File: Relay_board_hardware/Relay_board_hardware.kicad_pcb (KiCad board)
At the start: 2 copper layers, 101.6 x 101.6 mm, 25 parts, among them IC1 BTS3800SL, Q1 Q_NMOS_GDS, U1 Opamp_Dual

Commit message: moved trace and generated gerbs
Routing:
- net /RLY_V-: track 26.4 -> 27.3 mm
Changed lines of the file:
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@@
       (outputformat 1)
       (mirror false)
-      (drillshape 1)
+      (drillshape 0)
       (scaleselection 1)
-      (outputdirectory "")
+      (outputdirectory "gerbs/")
     )
   )
@@
     (fp_line (start 3.15 1.6) (end -3.15 1.6)
       (stroke (width 0.1) (type solid)) (layer "F.Fab"))
-    (pad "1" smd roundrect (at -3.05 0 180) (size 1.4 3.35) (layers "F.Cu" "F.Paste" "F.Mask") (roundrect_rratio 0.178571)
+    (pad "1" smd roundrect (at -3.05 0 180) (size 1.4 3.35) (layers "F.Cu" "F.Paste" "F.Mask") (roundrect_rratio 0.1785707143)
       (net 9 "Net-(U1A-+)") (pintype "passive"))
-    (pad "2" smd roundrect (at 3.05 0 180) (size 1.4 3.35) (layers "F.Cu" "F.Paste" "F.Mask") (roundrect_rratio 0.178571)
+    (pad "2" smd roundrect (at 3.05 0 180) (size 1.4 3.35) (layers "F.Cu" "F.Paste" "F.Mask") (roundrect_rratio 0.1785707143)
       (net 1 "GNDPWR") (pintype "passive"))
     (model "${KICAD6_3DMODEL_DIR}/Resistor_SMD.3dshapes/R_2512_6332Metric.wrl"
@@
     (fp_line (start 3.15 1.6) (end -3.15 1.6)
       (stroke (width 0.1) (type solid)) (layer "F.Fab"))
-    (pad "1" smd roundrect (at -3.05 0 180) (size 1.4 3.35) (layers "F.Cu" "F.Paste" "F.Mask") (roundrect_rratio 0.178571)
+    (pad "1" smd roundrect (at -3.05 0 180) (size 1.4 3.35) (layers "F.Cu" "F.Paste" "F.Mask") (roundrect_rratio 0.1785707143)
       (net 6 "VBUS") (pintype "passive"))
-    (pad "2" smd roundrect (at 3.05 0 180) (size 1.4 3.35) (layers "F.Cu" "F.Paste" "F.Mask") (roundrect_rratio 0.178571)
+    (pad "2" smd roundrect (at 3.05 0 180) (size 1.4 3.35) (layers "F.Cu" "F.Paste" "F.Mask") (roundrect_rratio 0.1785707143)
       (net 9 "Net-(U1A-+)") (pintype "passive"))
     (model "${KICAD6_3DMODEL_DIR}/Resistor_SMD.3dshapes/R_2512_6332Metric.wrl"
@@
     (fp_line (start 5.625 5) (end 5.625 -5)
       (stroke (width 0.1) (type solid)) (layer "B.Fab"))
-    (pad "1" smd roundrect (at -7.65 2.54 90) (size 4.6 1.1) (layers "B.Cu" "B.Paste" "B.Mask") (roundrect_rratio 0.227273)
+    (pad "1" smd roundrect (at -7.65 2.54 90) (size 4.6 1.1) (layers "B.Cu" "B.Paste" "B.Mask") (roundrect_rratio 0.2272727273)
       (net 13 "DSCHG_IN") (pinfunction "G") (pintype "input"))
-    (pad "2" smd roundrect (at -0.925 -2.775 90) (size 4.55 5.25) (layers "B.Cu" "B.Paste") (roundrect_rratio 0.054945)
+    (pad "2" smd roundrect (at -0.925 -2.775 90) (size 4.55 5.25) (layers "B.Cu" "B.Paste") (roundrect_rratio 0.05494505495)
       (net 10 "/PWRRES") (pinfunction "D") (pintype "passive"))
-    (pad "2" smd roundrect (at -0.925 2.775 90) (size 4.55 5.25) (layers "B.Cu" "B.Paste") (roundrect_rratio 0.054945)
+    (pad "2" smd roundrect (at -0.925 2.775 90) (size 4.55 5.25) (layers "B.Cu" "B.Paste") (roundrect_rratio 0.05494505495)
       (net 10 "/PWRRES") (pinfunction "D") (pintype "passive"))
-    (pad "2" smd roundrect (at 1.5 0 90) (size 9.4 10.8) (layers "B.Cu" "B.Mask") (roundrect_rratio 0.026596)
+    (pad "2" smd roundrect (at 1.5 0 90) (size 9.4 10.8) (layers "B.Cu" "B.Mask") (roundrect_rratio 0.02659595745)
       (net 10 "/PWRRES") (pinfunction "D") (pintype "passive"))
-    (pad "2" smd roundrect (at 3.925 -2.775 90) (size 4.55 5.25) (layers "B.Cu" "B.Paste") (roundrect_rratio 0.054945)
+    (pad "2" smd roundrect (at 3.925 -2.775 90) (size 4.55 5.25) (layers "B.Cu" "B.Paste") (roundrect_rratio 0.05494505495)
       (net 10 "/PWRRES") (pinfunction "D") (pintype "passive"))
-    (pad "2" smd roundrect (at 3.925 2.775 90) (size 4.55 5.25) (layers "B.Cu" "B.Paste") (roundrect_rratio 0.054945)
+    (pad "2" smd roundrect (at 3.925 2.775 90) (size 4.55 5.25) (layers "B.Cu" "B.Paste") (roundrect_rratio 0.05494505495)
       (net 10 "/PWRRES") (pinfunction "D") (pintype "passive"))
-    (pad "3" smd roundrect (at -7.65 -2.54 90) (size 4.6 1.1) (layers "B.Cu" "B.Paste" "B.Mask") (roundrect_rratio 0.227273)
+    (pad "3" smd roundrect (at -7.65 -2.54 90) (size 4.6 1.1) (layers "B.Cu" "B.Paste" "B.Mask") (roundrect_rratio 0.2272727273)
       (net 1 "GNDPWR") (pinfunction "S") (pintype "passive"))
     (model "${KICAD6_3DMODEL_DIR}/Package_TO_SOT_SMD.3dshapes/TO-263-2.wrl"
@@
   (segment (start 156.337 123.657) (end 156.754 123.24) (width 2.54) (layer "F.Cu") (net 7))
   (segment (start 156.337 133.9228) (end 156.337 123.657) (width 2.54) (layer "F.Cu") (net 7))
-  (segment (start 151.816 130.5698) (end 151.816 114.21) (width 2.54) (layer "F.Cu") (net 8))
-  (segment (start 151.816 114.21) (end 148.046 110.44) (width 2.54) (layer "F.Cu") (net 8))
-  (segment (start 148.463 133.9228) (end 151.816 130.5698) (width 2.54) (layer "F.Cu") (net 8))
+  (segment (start 152.908 129.4778) (end 152.908 115.302) (width 2.54) (layer "F.Cu") (net 8))
+  (segment (start 148.463 133.9228) (end 152.908 129.4778) (width 2.54) (layer "F.Cu") (net 8))
+  (segment (start 152.908 115.302) (end 148.046 110.44) (width 2.54) (layer "F.Cu") (net 8))
   (segment (start 163.195 95.25) (end 168.4 95.25) (width 0.254) (layer "F.Cu") (net 9))
   (segment (start 152.4 95.25) (end 147.195 95.25) (width 0.254) (layer "F.Cu") (net 9))

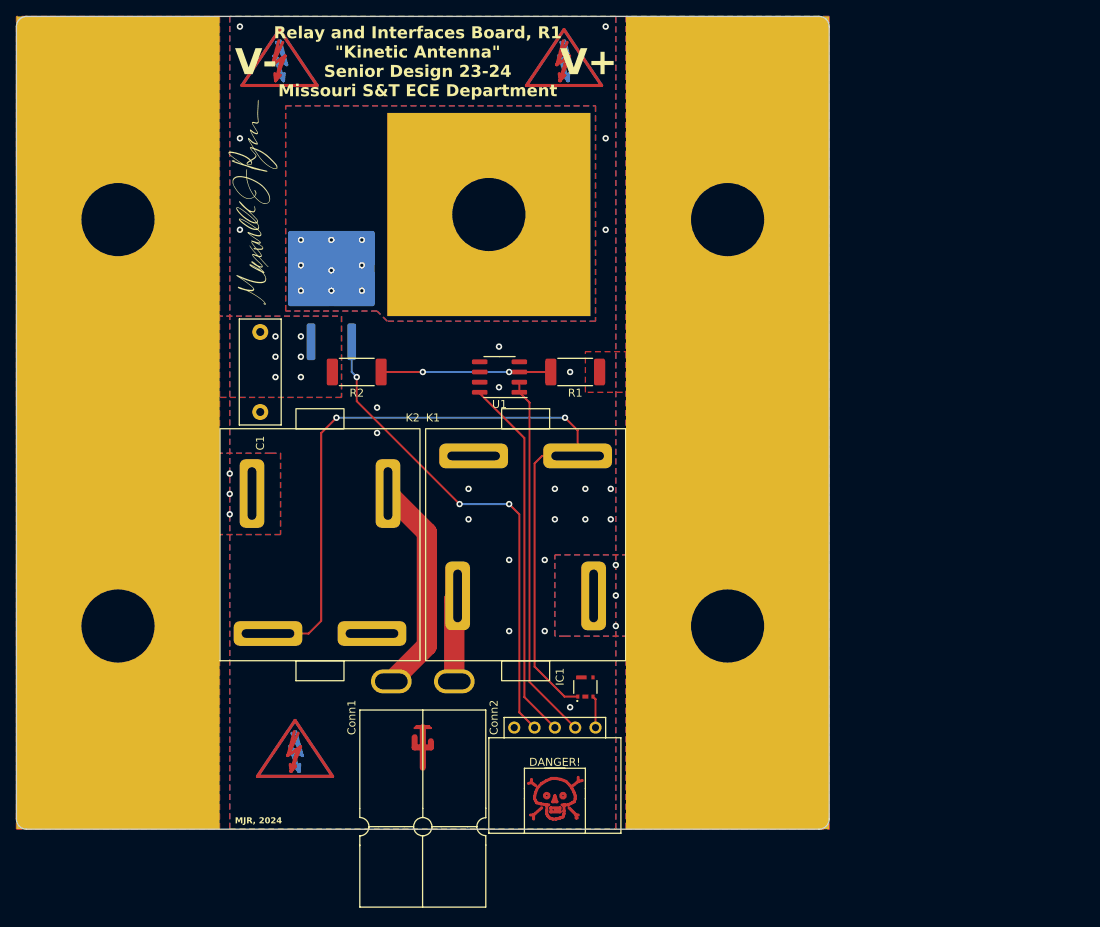
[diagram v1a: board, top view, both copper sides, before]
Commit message: 12V connection redesign
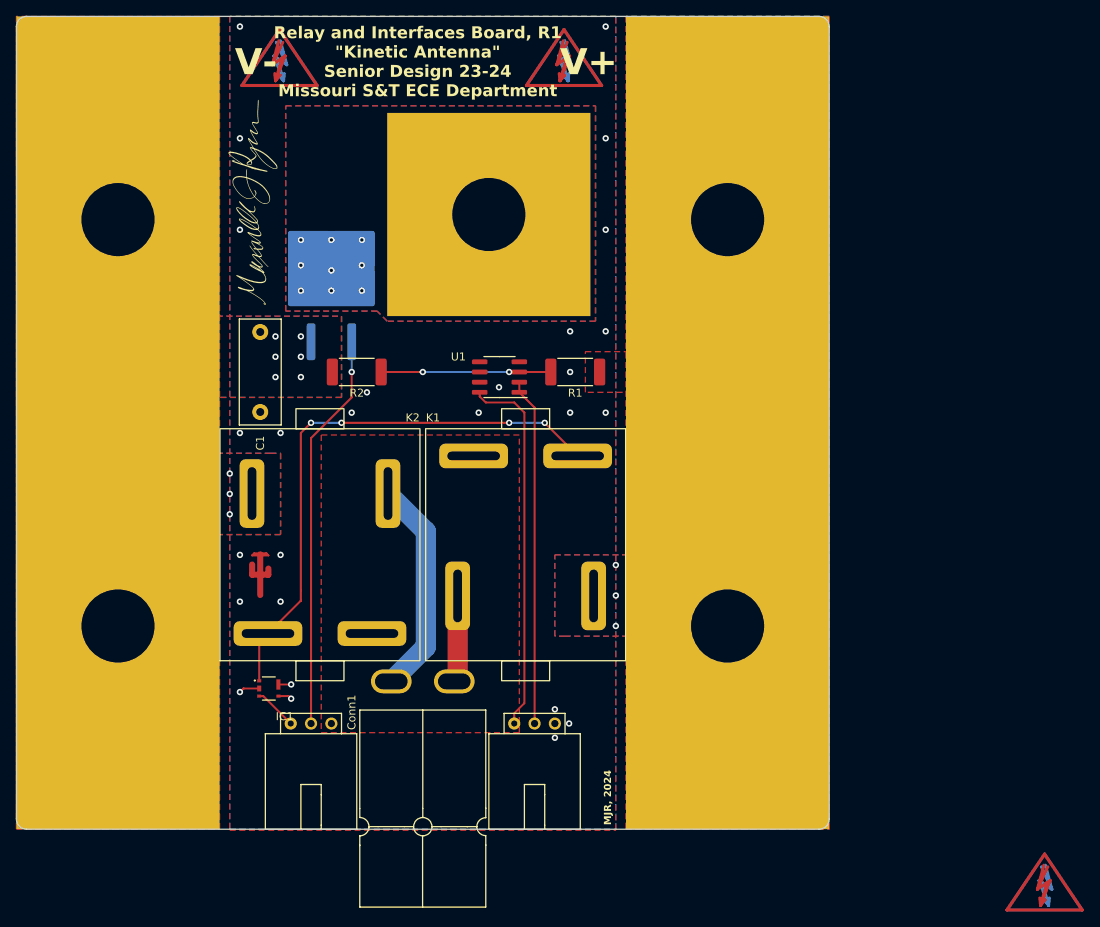
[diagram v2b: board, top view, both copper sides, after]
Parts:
- removed DANGER!: Symbol_Danger_CopperTop_Small, Symbol:Symbol_Danger_CopperTop_Small
- added Conn3: Molex_SL_03, 0-customs:MOLEX_SL_03_Horizontal, F.Cu at (141.0, 139.2)
- Conn2: value Molex_SL_05 -> Molex_SL_03; footprint 0-customs:MOLEX_SL_05_Horizontal -> 0-customs:MOLEX_SL_03_Horizontal
- Q1: value Q_NMOS_GDS -> IRF740ASPBF
- R1: value R -> 650k
- R2: value R -> 5k6
- U1: value Opamp_Dual -> MCP6497T-E/SN
- moved REF** 95.2 mm to (230.1, 159.7) (x2)
- moved IC1 39.6 mm to (133.2, 134.8), turned to -90 degrees
- moved REF** 29.6 mm to (132.1, 113.0)
- moved Conn2 5.11 mm to (168.9, 139.2)
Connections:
- Conn2 pad 1: RLY_IN -> GND
- IC1 pad 2: unconnected-(IC1-N.C._1-Pad2) -> GND
- IC1 pad 5: unconnected-(IC1-N.C._2-Pad5) -> GND
- K1 pad 1: GND -> +12V
- K2 pad 1: GND -> +12V
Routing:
- net Net-(IC1-DRAIN): track 105.6 -> 71.3 mm, vias 2 -> 4
- net DSCHG_IN: track 61.3 -> 49.8 mm, vias 3 -> 1
- net GND: track 0.00 -> 5.92 mm, vias 24 -> 27
- net /V_SENSE_OUT: track 46.1 -> 43.5 mm
- net RLY_IN: track 4.01 -> 5.36 mm
- net +3V3: track 45.8 -> 46.3 mm
- added copper zone on F.Cu, net +12V

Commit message: silkscreen updated, relay to rail plane dimensions confirmed, filecleanup,
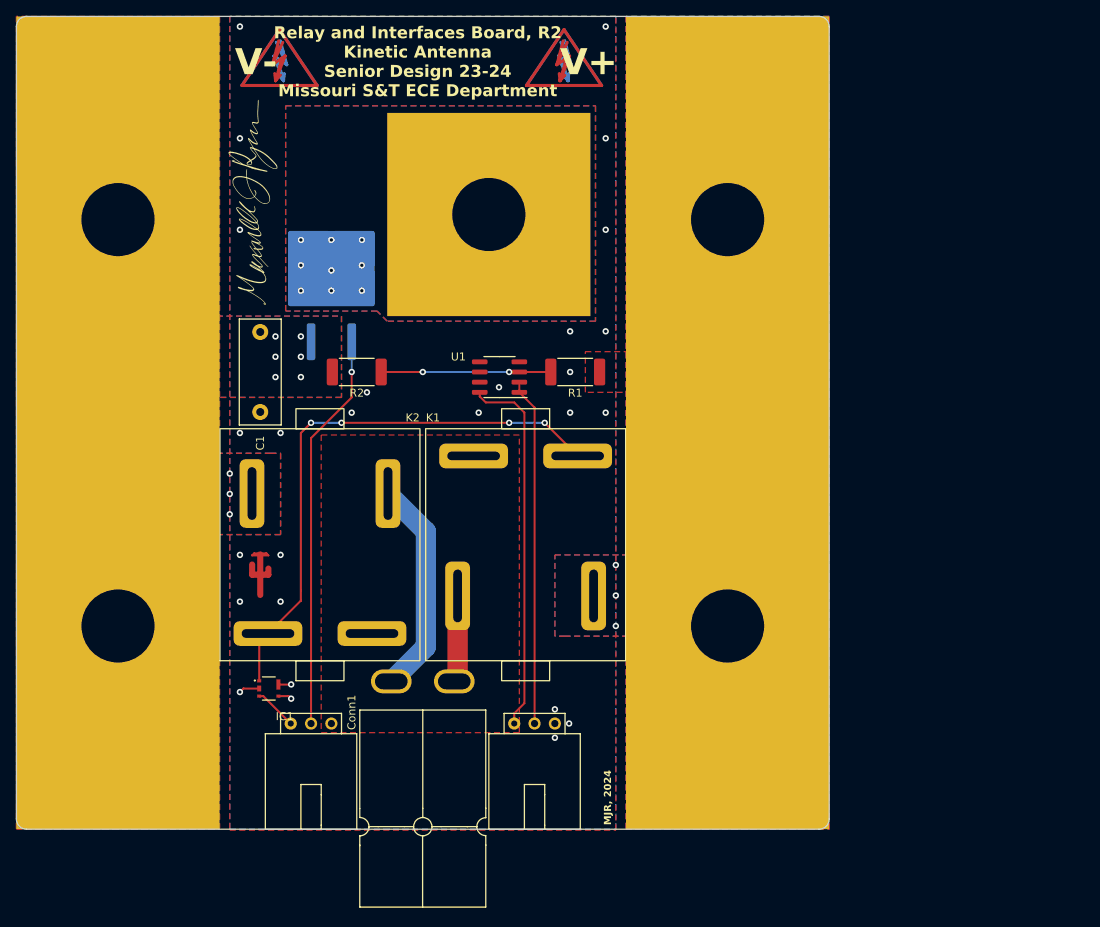
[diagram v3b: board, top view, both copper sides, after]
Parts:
- removed the G*** at (152.4, 55.9)
- removed the REF** at (230.1, 159.7) (x2)
- added G***: LOGO, MRDT_Silkscreens:yagi2_20mm, B.Cu at (152.4, 55.9)
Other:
- board text added: "Relay and Interfaces Board, R2 Kinetic Antenna Senior Design 23-24 Missouri S&T ECE Department"
- board text removed: "Relay and Interfaces Board, R1 {dblquote}Kinetic Antenna{dblquote} Senior Design 23-24 Missouri S&T ECE Department"

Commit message: R2 edits
gerbs generated
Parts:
- removed the REF** at (132.1, 113.0)
- added R3: 10k, Resistor_SMD:R_0603_1608Metric_Pad0.98x0.95mm_HandSolder, B.Cu at (145.2, 98.8)
- added U2: MCP1416, Package_TO_SOT_SMD:SOT-23-5, B.Cu at (141.5, 100.0)
- C1: value 4.7n -> 1u; footprint Capacitor_THT:C_Rect_L13.0mm_W5.0mm_P10.00mm_FKS3_FKP3_MKS4 -> Capacitor_SMD:C_0603_1608Metric_Pad1.08x0.95mm_HandSolder; moved to B.Cu
- U1: value MCP6497T-E/SN -> AD8541
- moved R2 19.9 mm to (163.8, 92.1)
- moved C1 17.6 mm to (144.1, 103.1), turned to 90 degrees
- moved Q1 3.75 mm to (141.5, 87.5)
- moved R1 3.38 mm to (172.6, 92.1)
- moved U1 1.27 mm to (162.0, 97.2)
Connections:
- C1 pad 1: GNDPWR -> +12V
- K2 pad 3: GNDPWR -> GND
- Q1 pad 1: DSCHG_IN -> Net-(Q1-G)
- Q1 pad 3: GNDPWR -> GND
- R2 pad 2: GNDPWR -> GND
- U1 pad 1: /V_SENSE_OUT -> (no net)
- U1 pad 6: (no net) -> /V_SENSE_OUT
- U1 pad 7: (no net) -> +3V3
- U1 pad 8: +3V3 -> (no net)
- V3 pad 1: GNDPWR -> GND
- V5 pad 1: GNDPWR -> GND
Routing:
- net +12V: track 0.00 -> 21.0 mm
- net Net-(U1A-+): track 21.2 -> 8.58 mm, vias 2 -> 0
- net DSCHG_IN: track 49.8 -> 39.6 mm, vias 1 -> 0
- net /V_SENSE_OUT: track 43.5 -> 47.9 mm
- net Net-(IC1-DRAIN): track 71.3 -> 69.3 mm, vias 4 -> 3
- net VBUS: vias 3 -> 5
- net GNDPWR: vias 9 -> 0
- net GND: vias 27 -> 22
- added copper zone on B.Cu, net +12V
- added copper zone on B.Cu, net Net-(Q1-G)
- removed copper zone on F.Cu, net +12V
- removed copper zone on B.Cu, net GNDPWR
- removed copper zone on F.Cu, net GNDPWR
